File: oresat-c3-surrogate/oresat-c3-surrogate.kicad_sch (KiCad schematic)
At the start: 38 parts, among them J1 J-SAMTEC-TFM-120-X1-XXX-D-RA, J2 Conn_01x04, J3 Terminal Block, J4 Barrel Jack, J5 Header, J6 Header, Q1 PMV45EN, Q2 DMP3050LVT-7, Q3 PMV45EN, Q4 DMP3050LVT-7, SW1 Slide Switch, SW2 Slide Switch, U1 Trinket-M0, U2 Seeed-USB-to-UART

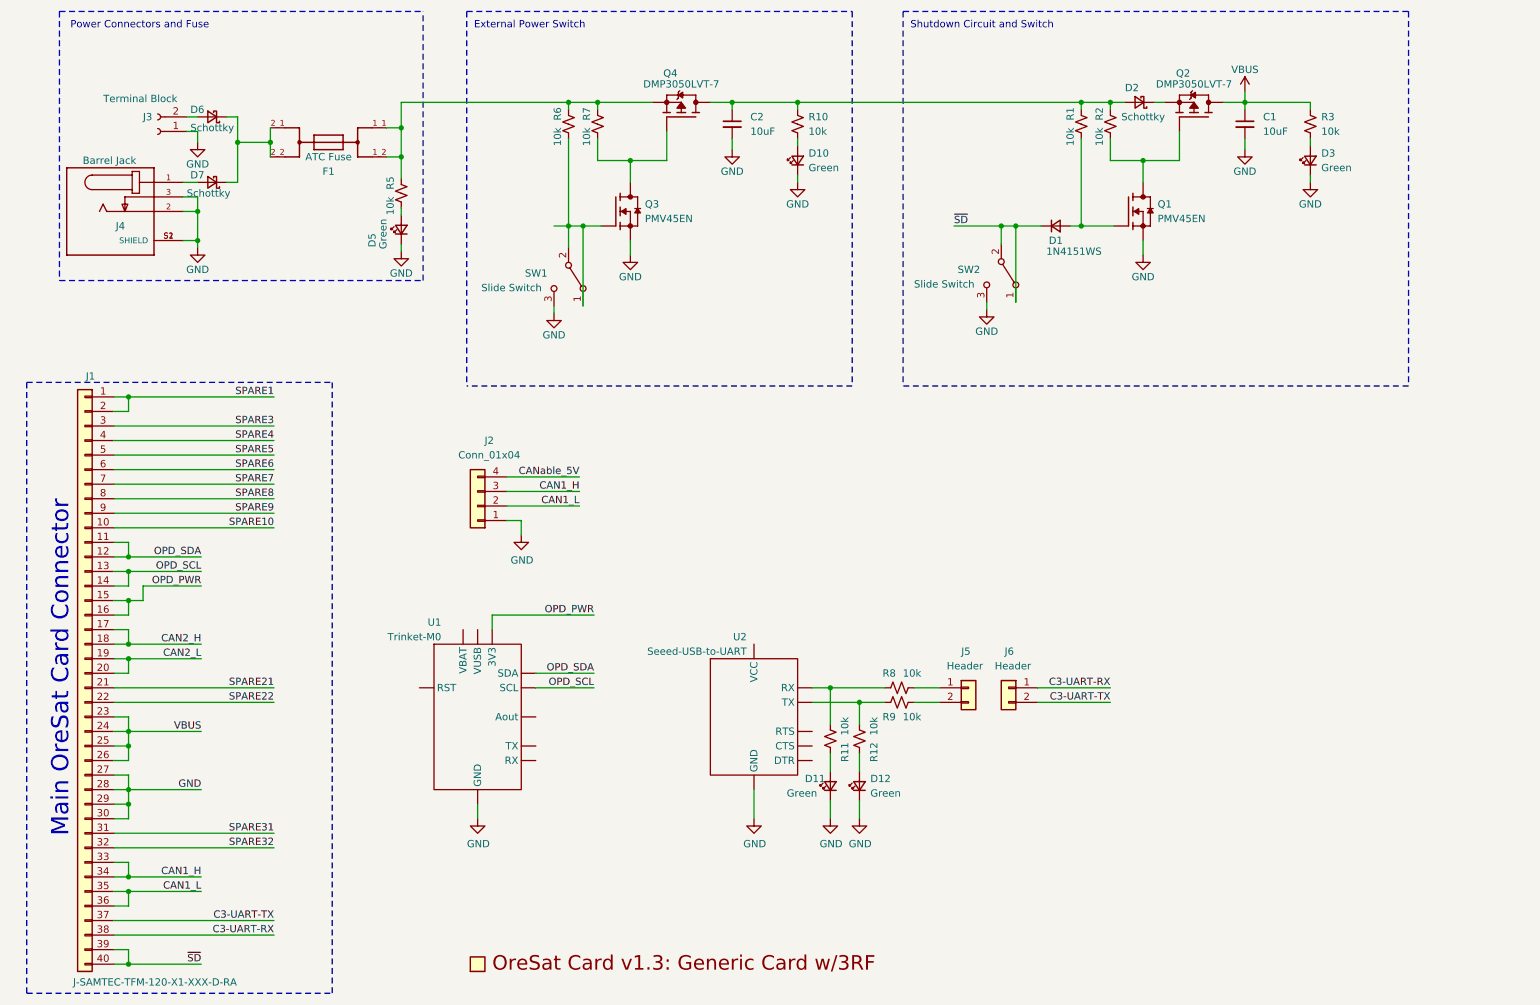
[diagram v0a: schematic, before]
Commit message: Updated schematic and finished board layout
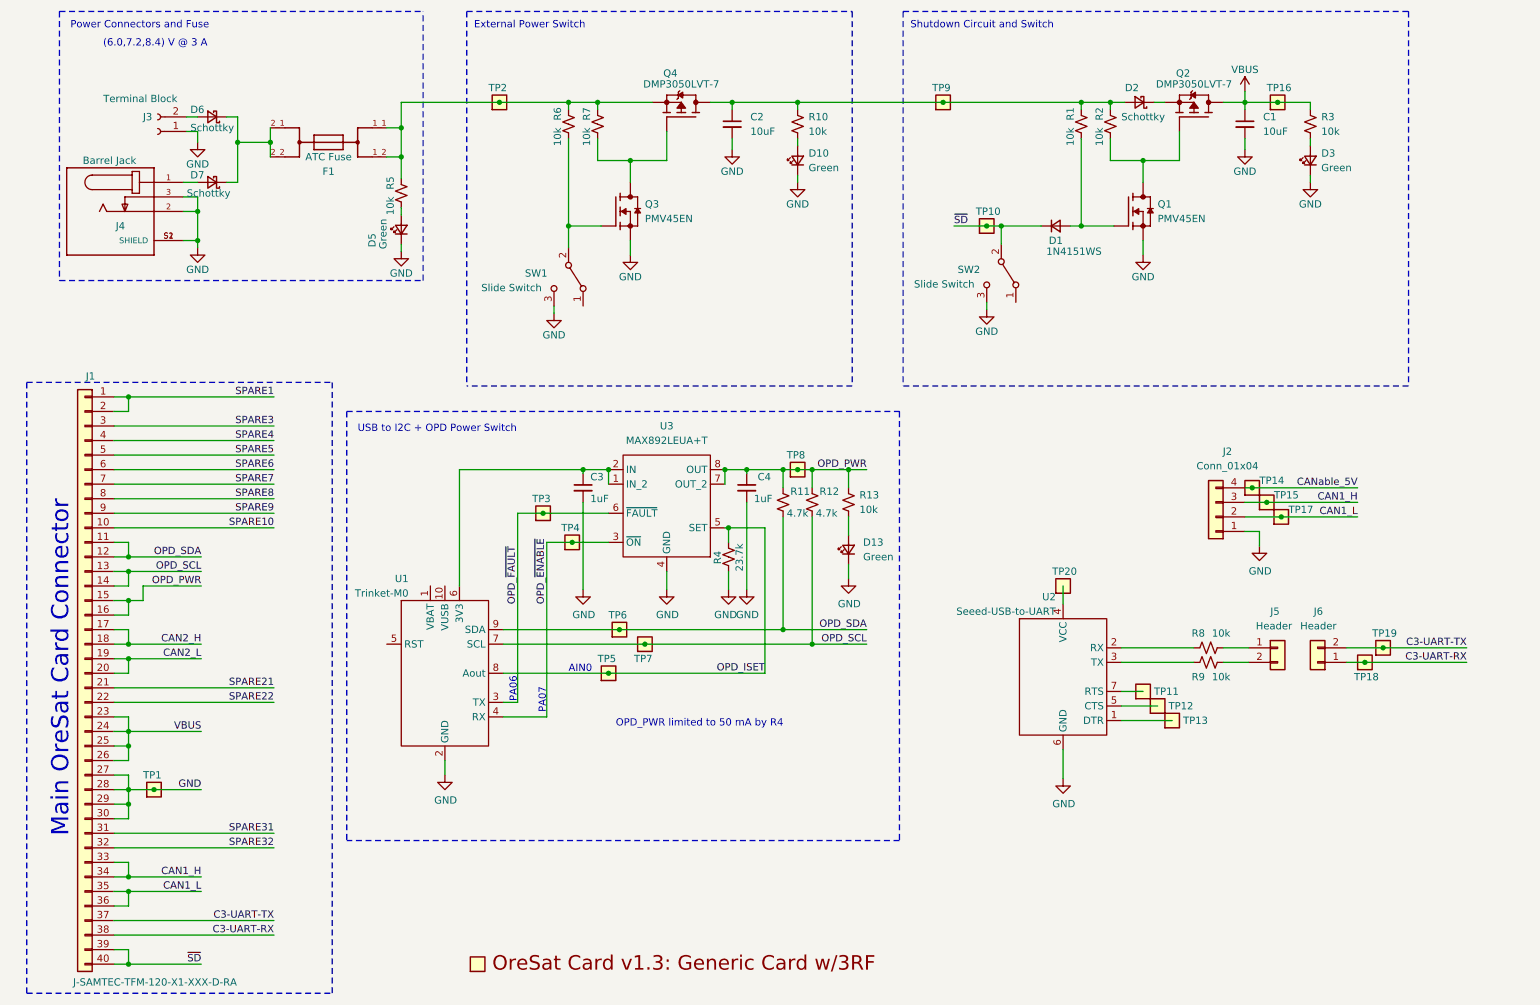
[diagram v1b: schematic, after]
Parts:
- removed D11, D12: Green, LED_SMD:LED_0603_1608Metric_Pad1.05x0.95mm_HandSolder, symbol Device:LED_Small
- added C3, C4: 1uF, Capacitor_SMD:C_0603_1608Metric_Pad1.08x0.95mm_HandSolder, symbol Device:C_Small
- added D13: Green, LED_SMD:LED_0603_1608Metric_Pad1.05x0.95mm_HandSolder, symbol Device:LED_Small
- added R13: 10k, Resistor_SMD:R_0603_1608Metric_Pad0.98x0.95mm_HandSolder, symbol Device:R_Small_US
- added R4: 23.7k, Resistor_SMD:R_0603_1608Metric_Pad0.98x0.95mm_HandSolder, symbol Device:R_Small_US
- added TP1, TP10, TP11, TP12, TP13, TP14, TP15, TP16, TP17, TP18, TP19, TP2, TP20, TP3, TP4, TP5, TP6, TP7, TP8, TP9: TEST-POINT-LARGE-SQUARE, 1X01, symbol oresat-misc:TEST-POINT-LARGE-SQUARE
- added U3: MAX892LEUA+T, U-Maxim-MAX892LEUA+T-power-switch:MAX892LEUA+T, symbol U-Maxim-MAX892LEUA+T-power-switch:MAX892LEUA+T
- J5, J6: footprint Connector_PinHeader_2.54mm:PinHeader_1x02_P2.54mm_Vertical -> Connector_PinHeader_2.54mm:PinHeader_1x02_P2.54mm_Horizontal
- R11, R12: value 10k -> 4.7k
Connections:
- net C3-UART-RX: now also TP18.1
- net C3-UART-TX: now also TP19.1
- net CAN1_H: now also TP15.1
- net CAN1_L: now also TP17.1
- net CANable_5V: now also TP14.1
- net GND: now also C3.2, C4.2, D13.1 (K), R4.2, TP1.1, U3.4 (GND)
- net OPD_PWR: now also R11.1, R12.1, C4.1, R13.1, TP8.1, U3.7 (OUT_2), U3.8 (OUT); no longer U1.6 (3V3)
- net OPD_SCL: now also R12.2, TP7.1
- net OPD_SDA: now also R11.2, TP6.1
- net VBUS: now also TP16.1
- net ~{SD}: now also TP10.1; no longer SW2.1 (A)
- net at Q3.1, R6.2, SW1.2 (B): no longer SW1.1 (A)
- net at R9.1, U2.3 (TX): no longer R12.2
- net at C2.1, D2.2 (A), Q4.1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: now also TP9.1
- net OPD_~{FAULT}: now reaches U1.3 (TX)
- net OPD_~{FAULT}: now also TP3.1, U3.6 (~{FAULT})
- net OPD_~{ENABLE}: now reaches U1.4 (RX)
- net OPD_~{ENABLE}: now also TP4.1, U3.3 (~{ON})
- net OPD_ISET: now reaches U1.8 (Aout)
- net OPD_ISET: now also R4.1, TP5.1, U3.5 (SET)
- net at F1.1_1, F1.1_2, Q4.4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: now also TP2.1
- net at R8.1, U2.2 (RX): no longer R11.2
- net at U2.1 (DTR): now also TP13.1
- net at U2.4 (VCC): now also TP20.1
- net at U2.5 (CTS): now also TP12.1
- net at U2.7 (RTS): now also TP11.1
- new net: C3.1, U1.6 (3V3), U3.1 (IN_2), U3.2 (IN)
- new net: D13.2 (A), R13.2
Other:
- note added: "(6.0,7.2,8.4) V @ 3 A"
- note added: "AIN0"
- note added: "OPD_PWR limited to 50 mA by R4"
- note added: "PA06"
- note added: "PA07"
- note added: "USB to I2C + OPD Power Switch"
- moved on the sheet: J2, J5, J6, R8, R9

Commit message: Updated surrogate board. Moved D2 on schematic, fixed UART pin headers, rotated fuse holder.
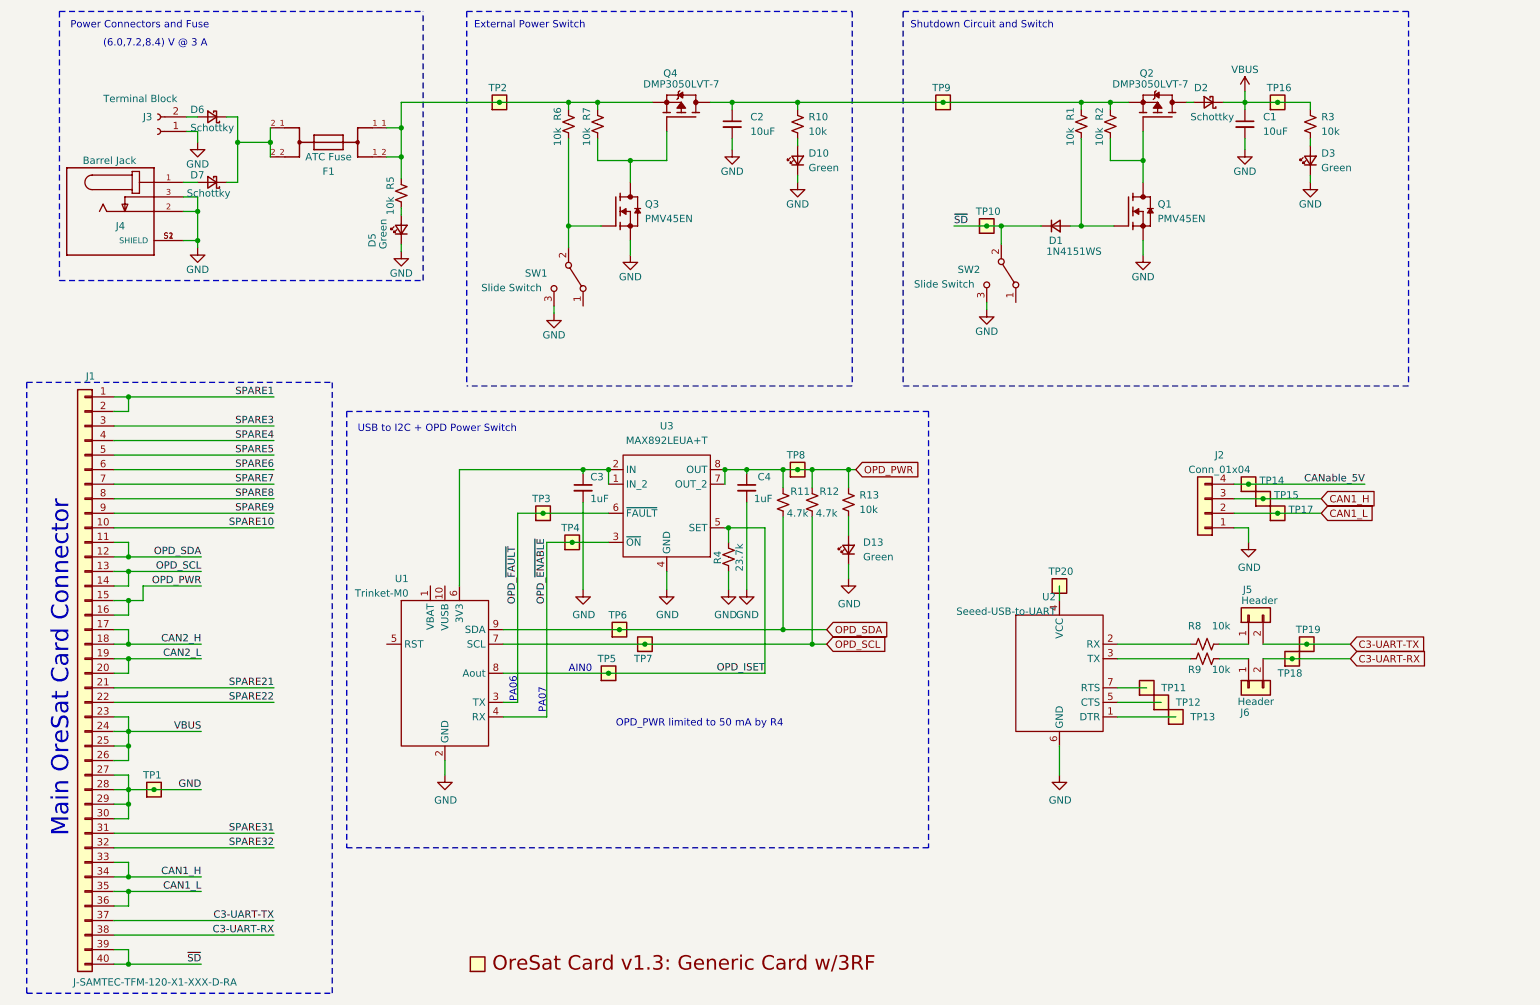
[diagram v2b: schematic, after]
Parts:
- C1, C2: DIST (none) -> Digi-Key; DPN (none) -> 490-10475-1-ND; MFR (none) -> Murata; MPN (none) -> GRM188R61A106ME69D
- C3, C4: DIST (none) -> Digi-Key; DPN (none) -> 490-GCM188R71E105KA64JCT-ND; MFR (none) -> Murata; MPN (none) -> GCM188R71E105KA64J
- D1: DIST (none) -> Digi-Key; DPN (none) -> 112-1N4151WS-E3-08CT-ND; MFR (none) -> Vishay; MPN (none) -> 1N4151WS-E3-08
- D10, D13, D3, D5: DIST (none) -> Digi-Key; DPN (none) -> 1830-1062-1-ND; MFR (none) -> Inolux; MPN (none) -> IN-S63AT5G
- D2, D6, D7: footprint Diode_SMD:D_SMB -> Diode_SMD:D_SMA; DIST (none) -> Digi-Key; DPN (none) -> SSA33L-E3/61TGICT-ND; MFR (none) -> Vishay; MPN (none) -> SSA33L-E3/61T
- F1: DIST (none) -> Digi-Key; DPN (none) -> 36-3550-2-ND; MFR (none) -> Keystone; MPN (none) -> 3550-2
- J1: DIST (none) -> Digi-Key; DPN (none) -> SAM10145-ND; MFR (none) -> Samtec; MPN (none) -> TFM-120-01-L-D-RA
- J2: DIST (none) -> Digi-Key; DPN (none) -> WM12840-ND; MFR (none) -> Molex; MPN (none) -> 0757570441
- J3: DIST (none) -> Digi-Key; DPN (none) -> 277-6718-ND; MFR (none) -> Phoenix Contact; MPN (none) -> 1995499
- J4: DIST (none) -> Digi-Key; DPN (none) -> CP-051AH-ND; MFR (none) -> CUI Devices; MPN (none) -> PJ-051AH
- J5, J6: DIST (none) -> Digi-Key; DPN (none) -> 2057-PH1RB-02-UA-ND; MFR (none) -> Tech; MPN (none) -> PH1RB-02-UA
- Q1, Q3: DIST (none) -> Digi-Key; DPN (none) -> 1727-2307-1-ND; MFR (none) -> Nexperia; MPN (none) -> PMV45EN2R
- Q2, Q4: DIST (none) -> Digi-Key; MFR (none) -> Diodes Incorporated
- R1, R10, R13, R2, R3, R5, R6, R7, R8, R9: DIST (none) -> Digi-Key; DPN (none) -> RNCF0603BTE10K0CT-ND; MFR (none) -> Stackpole; MPN (none) -> RNCF0603BTE10K0
- R11, R12: DIST (none) -> Digi-Key; DPN (none) -> RMCF0603FT4K70CT-ND; MFR (none) -> Stackpole; MPN (none) -> RMCF0603FT4K70
- R4: DIST (none) -> Digi-Key; DPN (none) -> RMCF0603FT23K7CT-ND; MFR (none) -> Stackpole; MPN (none) -> RMCF0603FT23K7
- SW1, SW2: DIST (none) -> Digi-Key; DPN (none) -> 401-2012-1-ND; MFR (none) -> C&K; MPN (none) -> AYZ0102AGRLC
- TP1, TP10, TP11, TP12, TP13, TP14, TP15, TP16, TP17, TP18, TP19, TP2, TP20, TP3, TP4, TP5, TP6, TP7, TP8, TP9: footprint 1X01 -> oresat-misc:1X01
- U1: DIST (none) -> Digi-Key; DPN (none) -> 1528-2361-ND; MFR (none) -> Adafruit; MPN (none) -> 3500
- U2: DIST (none) -> Digi-Key; DPN (none) -> 1597-1332-ND; MFR (none) -> Seeed; MPN (none) -> 103990049
- U3: DIST (none) -> Digi-Key; DPN (none) -> MAX892LEUA+-ND; MFR (none) -> Maxim; MPN (none) -> MAX892LEUA+
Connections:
- net C3-UART-RX: now also J6.2 (Pin_2); no longer J6.1 (Pin_1)
- net C3-UART-TX: now also J5.2 (Pin_2); no longer J6.2 (Pin_2)
- net VBUS: now also D2.1 (K); no longer Q2.1, Q2.2, Q2.5, Q2.6
- net at C2.1, Q4.1, Q4.2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: now also Q2.4; no longer D2.2 (A)
- net at R9.2: now also J6.1 (Pin_1); no longer J5.2 (Pin_2)
- new net: D2.2 (A), Q2.1, Q2.2, Q2.5, Q2.6
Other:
- moved on the sheet: D2, J2, J5, J6, Q2, R8, R9, TP11, TP12, TP13, TP14, TP15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

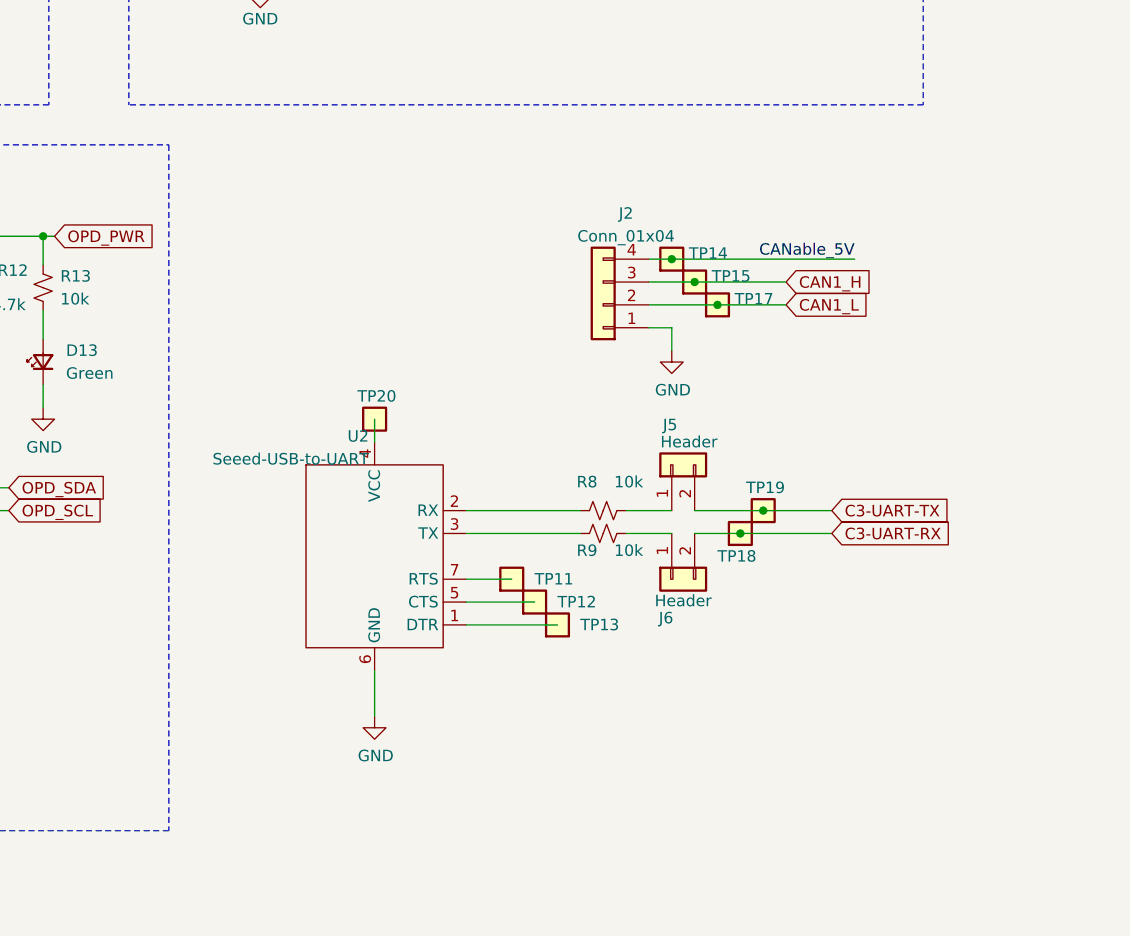
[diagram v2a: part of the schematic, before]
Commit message: Updated BOM during first order, cleaned up some very trivial things on schematic.
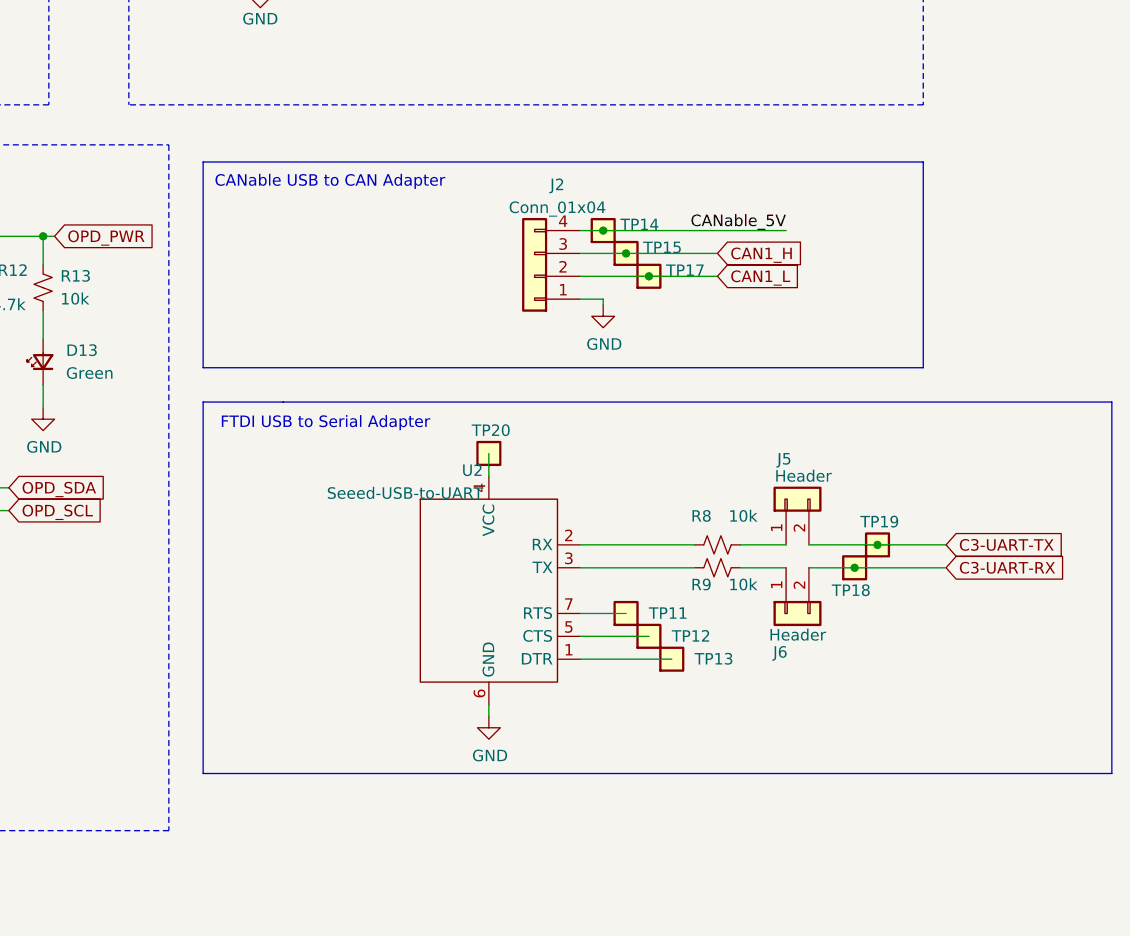
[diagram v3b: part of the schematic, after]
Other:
- note added: "CANable USB to CAN Adapter"
- note added: "FTDI USB to Serial Adapter"
- moved on the sheet: J2, J5, J6, R8, R9, TP11, TP12, TP13, TP14, TP15, TP17, TP18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
